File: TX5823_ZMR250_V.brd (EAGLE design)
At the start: 66.7 x 42 mm, 53 parts, among them IC1 REG1117, X1 LTI-SASF54GT

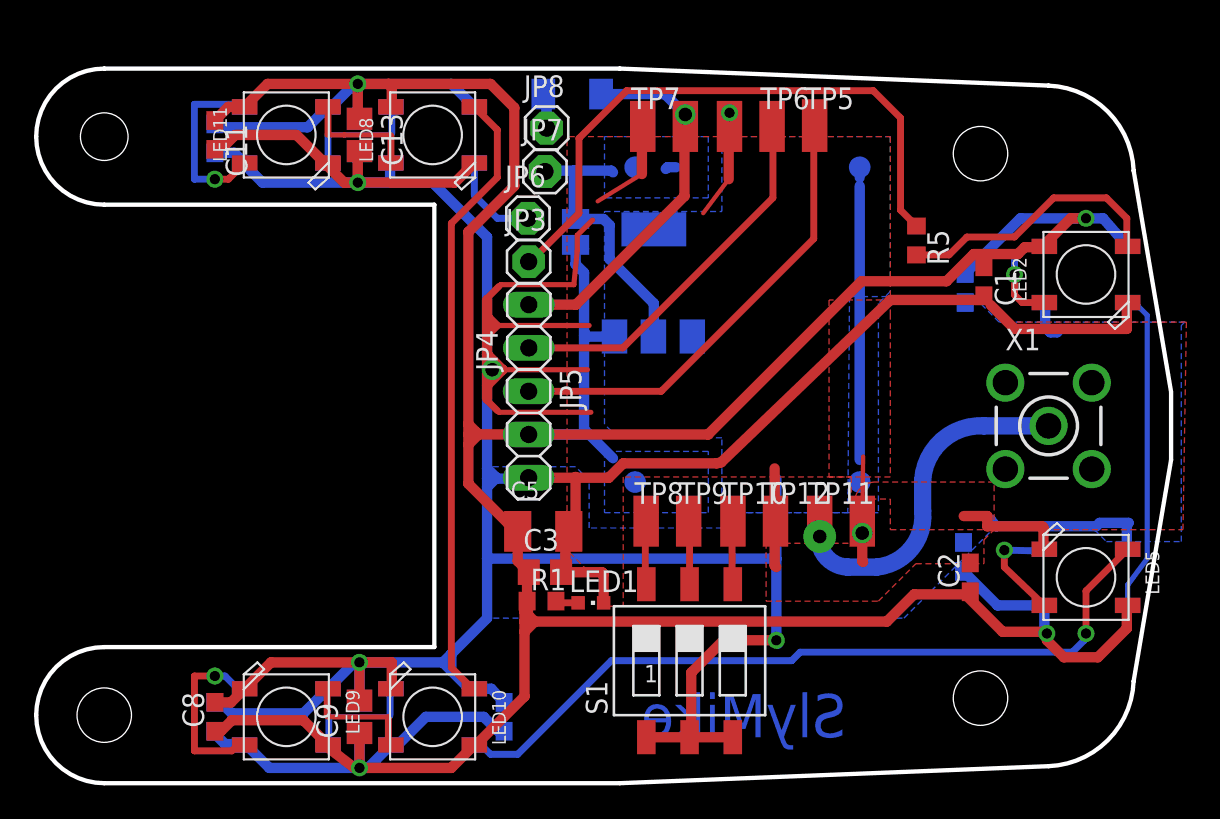
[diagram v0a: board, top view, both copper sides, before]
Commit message: Add files via upload
Moved a few parts, changed some via sizes, deleted a capacitor and added more test points for switch mode PSU.
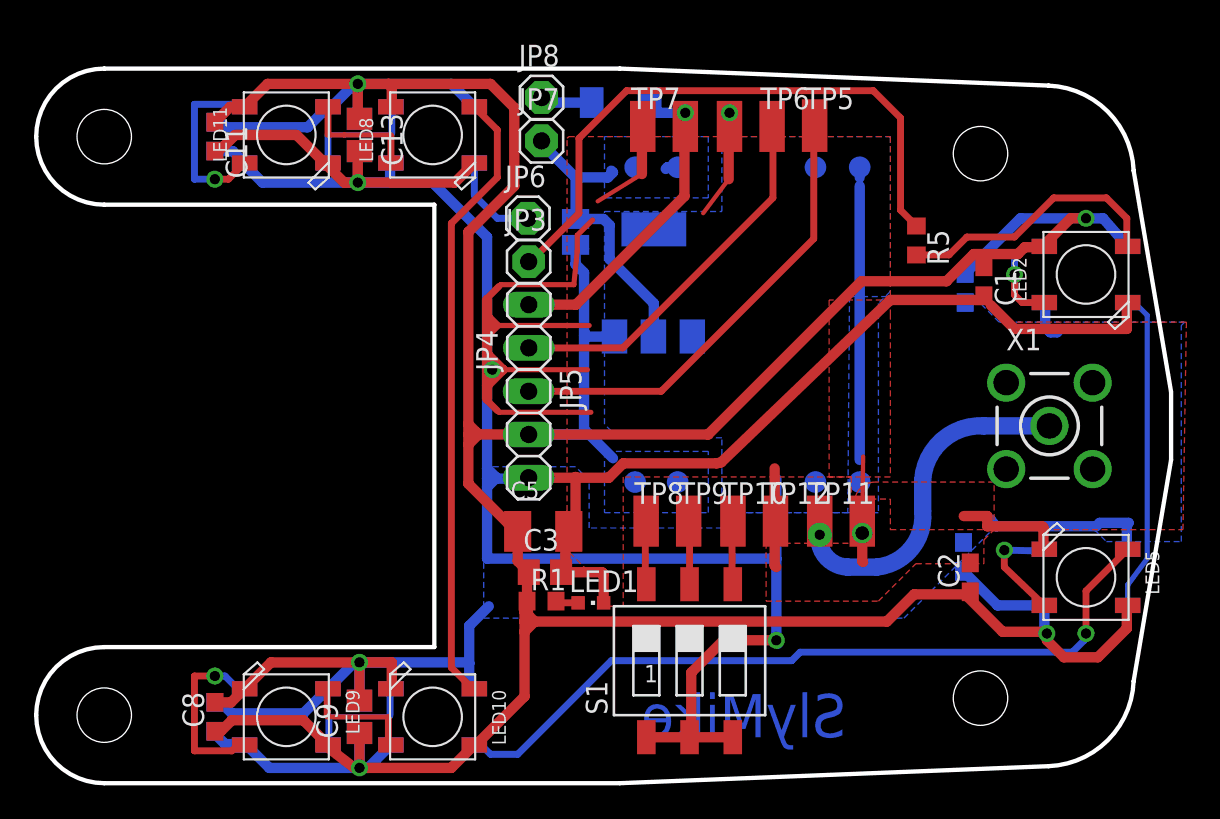
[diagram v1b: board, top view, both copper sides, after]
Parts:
- removed C10: (no value), rcl:C0603
- added TP13, TP14, TP15, TP16: TPB1,27, testpad:B1,27
- moved R2 2.89 mm to (36.6, 41.9)
- moved JP8 1.82 mm to (32.0, 42.2)
- moved JP7 1.81 mm to (32.0, 39.6)
- moved C11 0.10 mm to (12.8, 39.9)
- moved C12 0.10 mm to (12.8, 39.9)
- moved X1 0.05 mm to (61.9, 22.9)
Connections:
- net +5V: now also TP15.TP; no longer C10.1
- net 3V3OUT: now also TP16.TP
- net GND: now also TP13.TP, TP14.TP; no longer C10.2
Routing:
- net +5V: track 252.9 -> 245.7 mm
- net GND: track 316.8 -> 311.3 mm
- net +3V3: track 21.2 -> 18.6 mm
- net N$4: track 4.11 -> 3.07 mm
- net 3V3OUT: track 18.1 -> 18.9 mm
